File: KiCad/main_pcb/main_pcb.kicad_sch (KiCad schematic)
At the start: 14 parts, among them U4 SD Card Socket, U5 TI TXB0104DR, U6 TI TXB0104DR, U7 TI TXB0104DR, U9 ILI9488

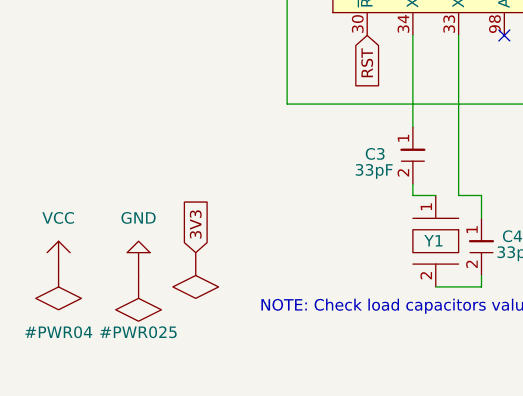
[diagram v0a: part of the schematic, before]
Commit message: feat(KiCad): Continues work on main PCB circuit
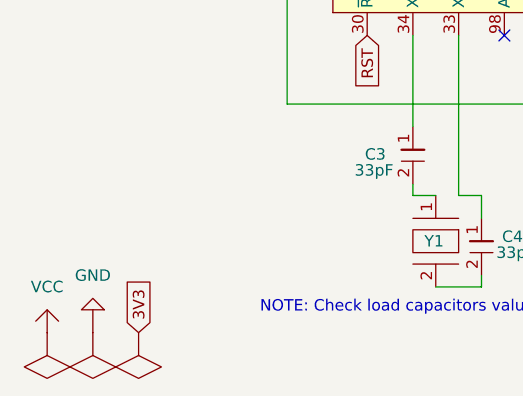
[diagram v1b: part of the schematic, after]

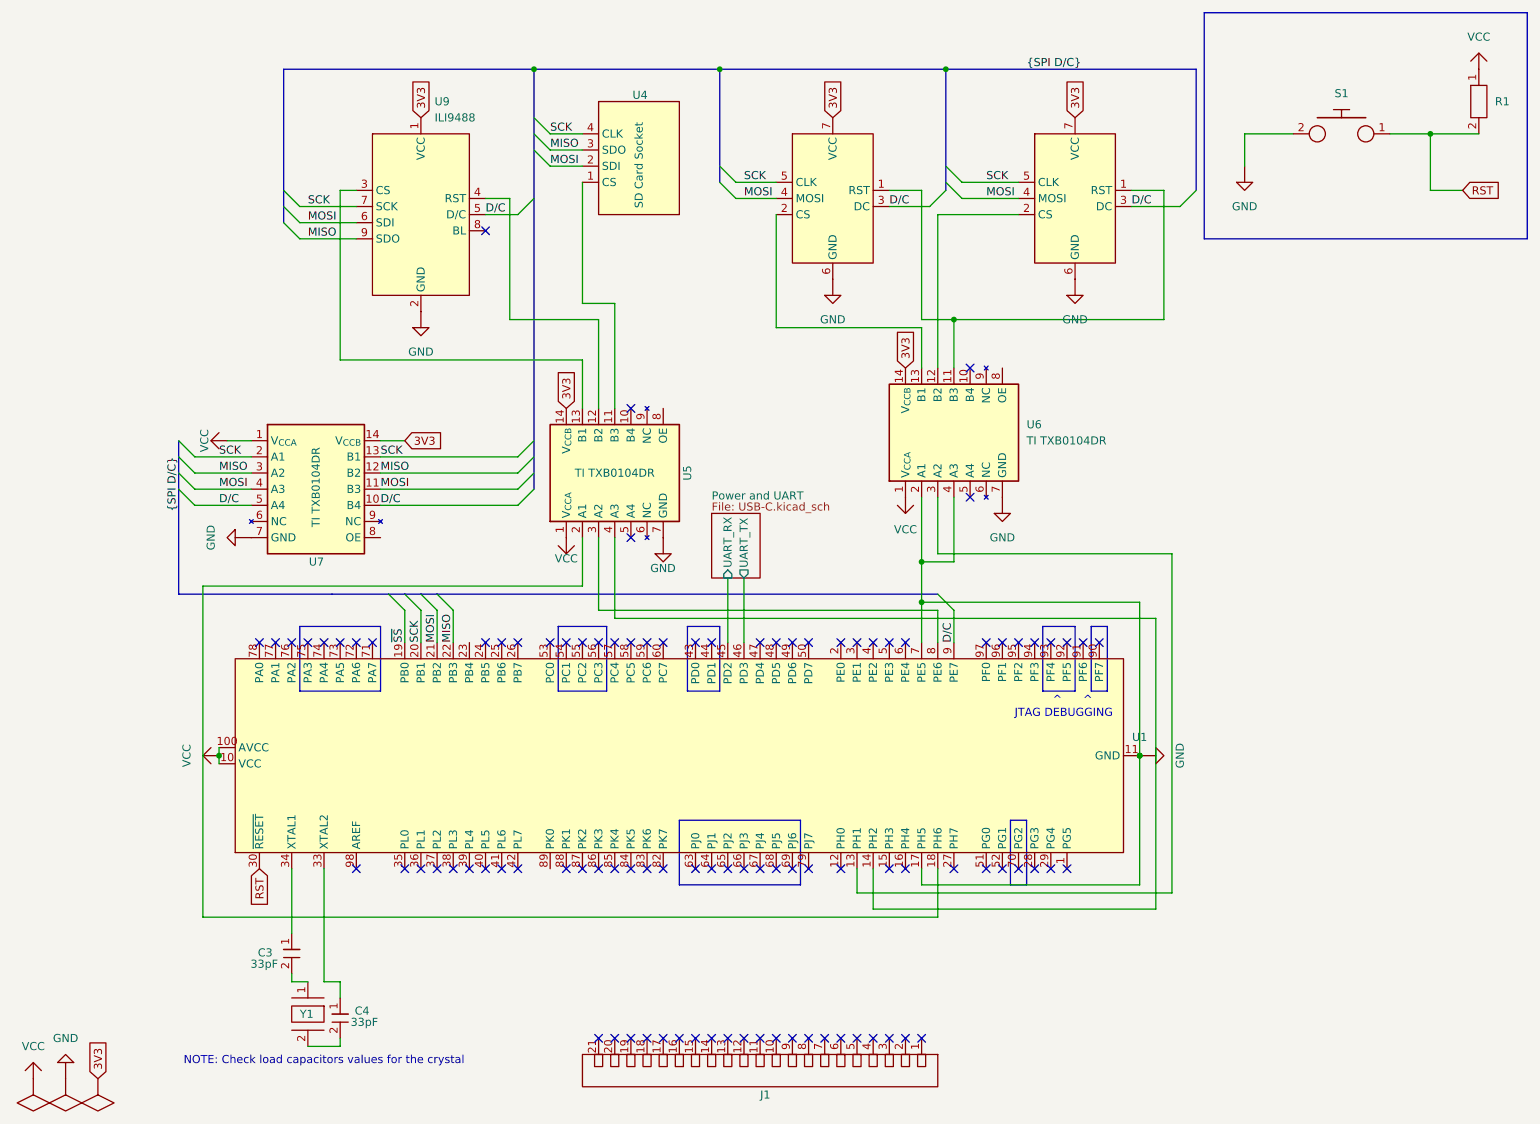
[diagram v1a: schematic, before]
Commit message: feat(KiCad): Continues work on main PCB circuit
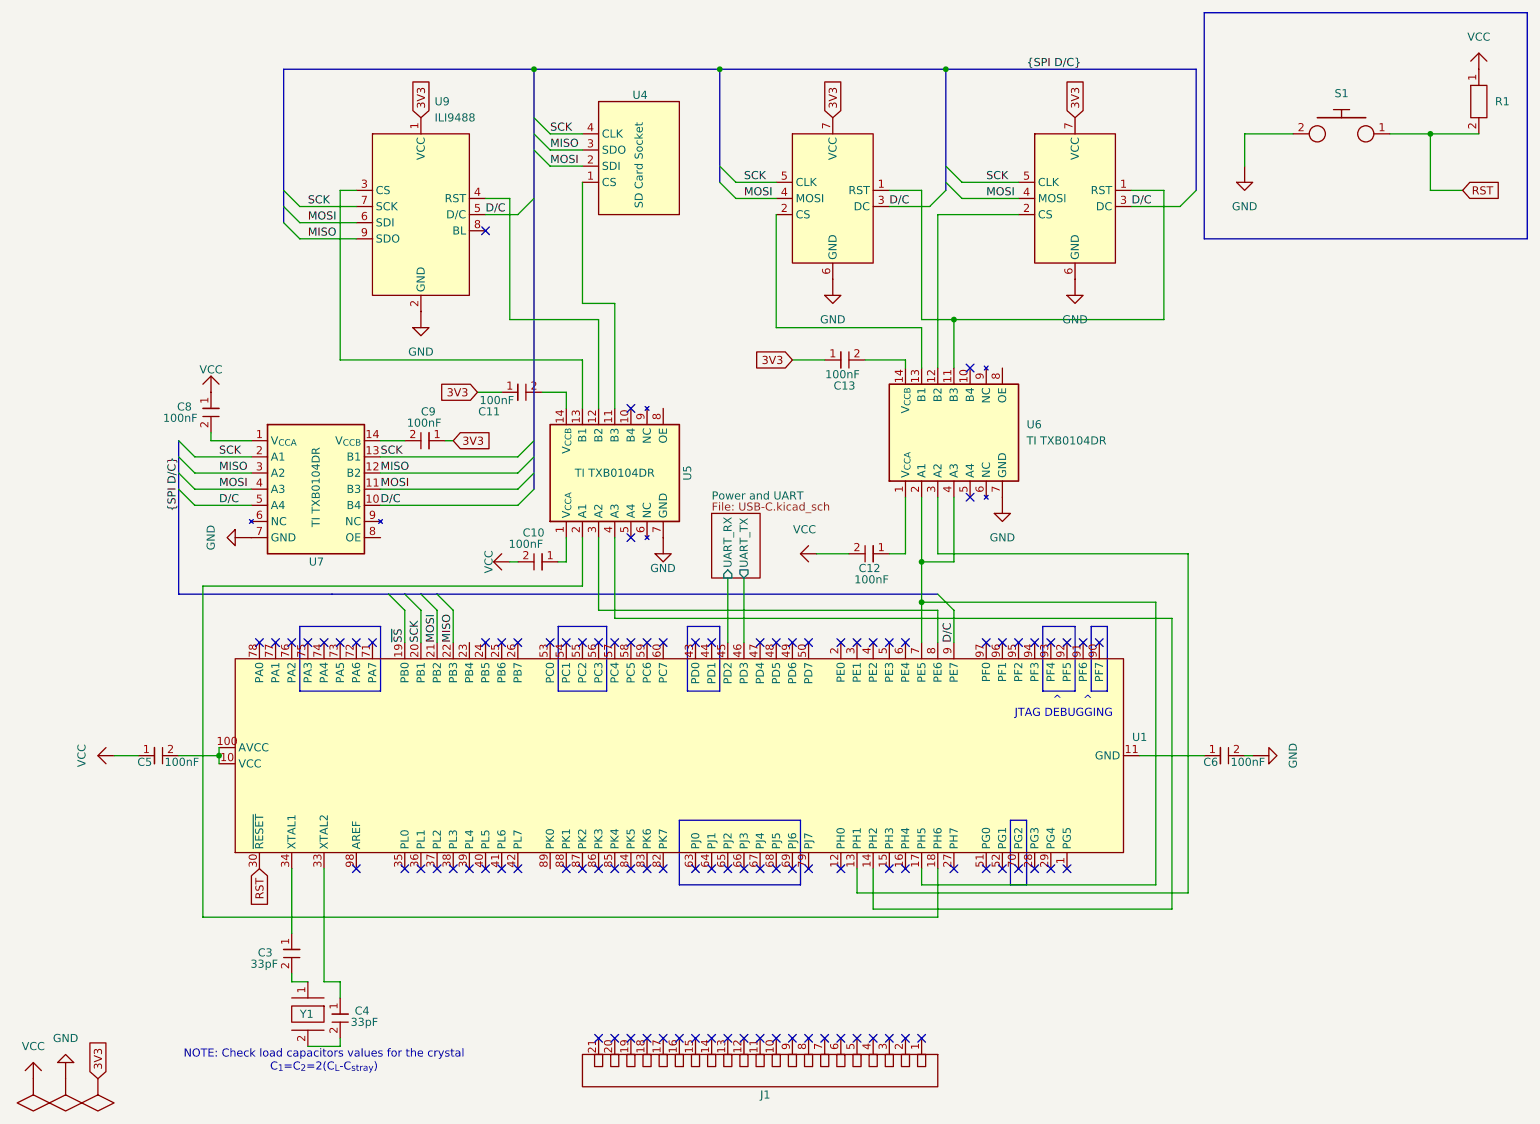
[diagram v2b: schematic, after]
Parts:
- added C10, C11, C12, C13, C5, C6, C8, C9: 100nF, symbol Lily's_Pad:Capacitor
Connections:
- net 3V3: now also C11.1, C13.1, C9.1; no longer U5.14 (V_{CCB}), U6.14 (V_{CCB}), U7.14 (V_{CCB})
- net GND: now also C6.1, C6.2; no longer U1.17 (PH5), U1.7 (PE5), U6.2 (A1), U6.4 (A3)
- net VCC: now also C10.2, C12.2, C5.1, C5.2, C8.1; no longer U5.1 (V_{CCA}), U6.1 (V_{CCA}), U7.1 (V_{CCA})
- new net: C8.2, U7.1 (V_{CCA})
- new net: C9.2, U7.14 (V_{CCB})
- new net: C11.2, U5.14 (V_{CCB})
- new net: C12.1, U6.1 (V_{CCA})
- new net: C10.1, U5.1 (V_{CCA})
- new net: C13.2, U6.14 (V_{CCB})
- new net: U1.17 (PH5), U1.7 (PE5), U6.2 (A1), U6.4 (A3)
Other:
- note added: "NOTE: Check load capacitors values for the crystal C_{1}=C_{2}=2(C_{L}-C_{stray})"
- note removed: "NOTE: Check load capacitors values for the crystal"

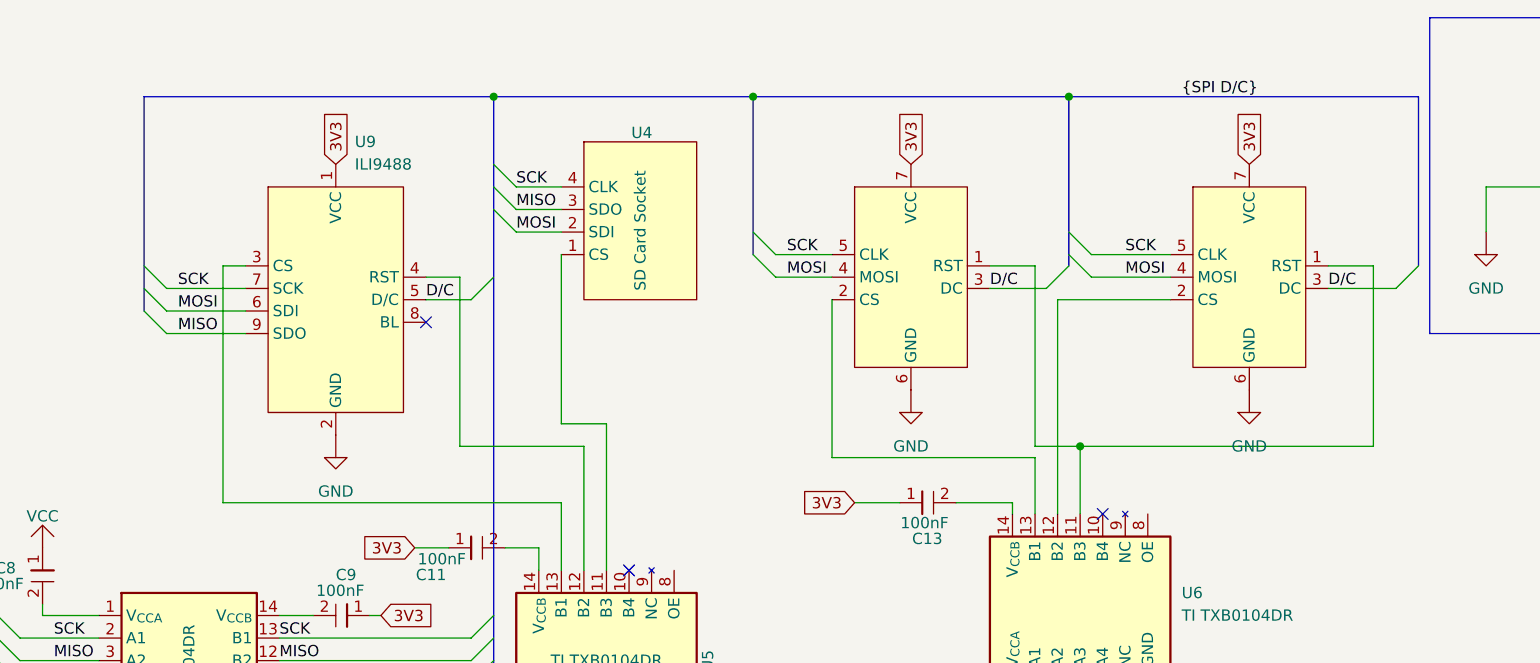
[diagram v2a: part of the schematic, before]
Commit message: feat(KiCad): Continues work on main PCB circuit
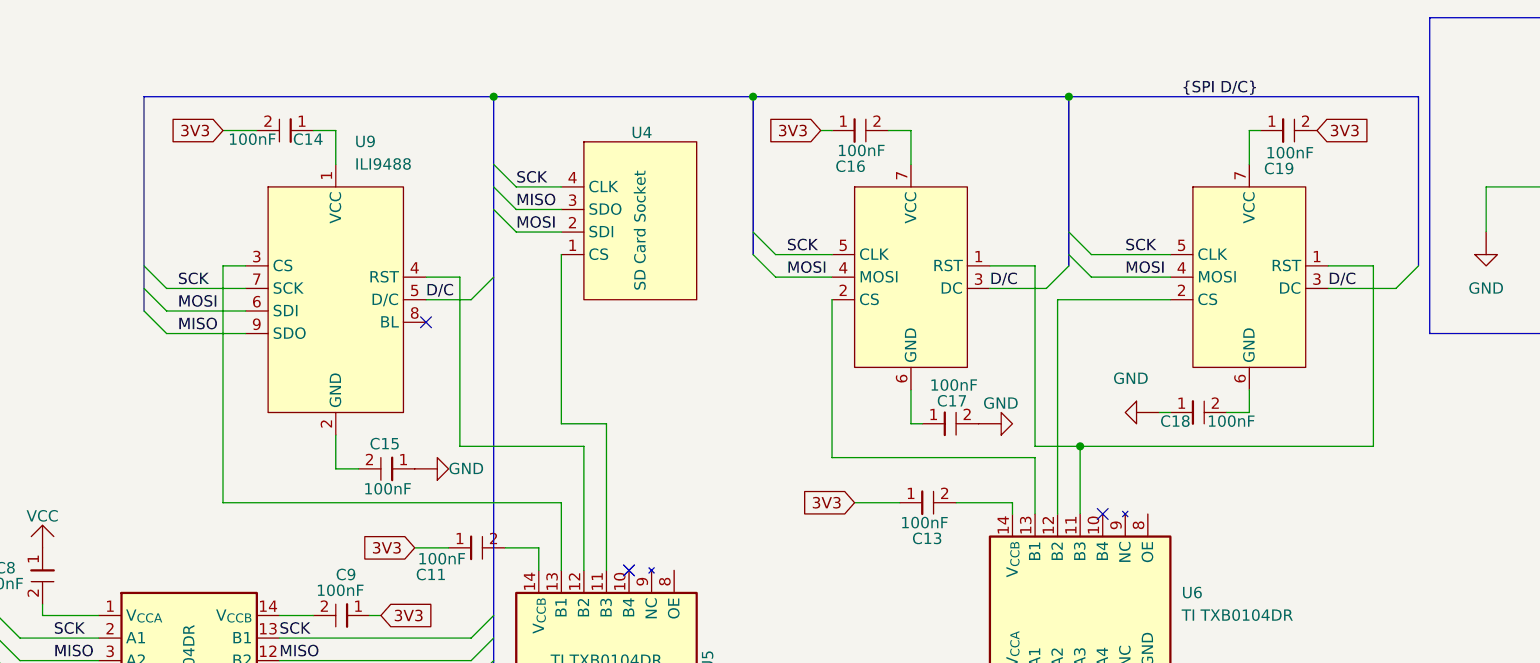
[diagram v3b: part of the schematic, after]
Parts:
- added C14, C15, C16, C17, C18, C19: 100nF, symbol Lily's_Pad:Capacitor
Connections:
- net 3V3: now also C14.2, C16.1, C19.2; no longer U2.7 (VCC), U3.7 (VCC), U9.1 (VCC)
- net GND: now also C15.1, C17.2, C18.1; no longer U2.6 (GND), U3.6 (GND), U9.2 (GND)
- new net: C18.2, U2.6 (GND)
- new net: C19.1, U2.7 (VCC)
- new net: C17.1, U3.6 (GND)
- new net: C16.2, U3.7 (VCC)
- new net: C14.1, U9.1 (VCC)
- new net: C15.2, U9.2 (GND)

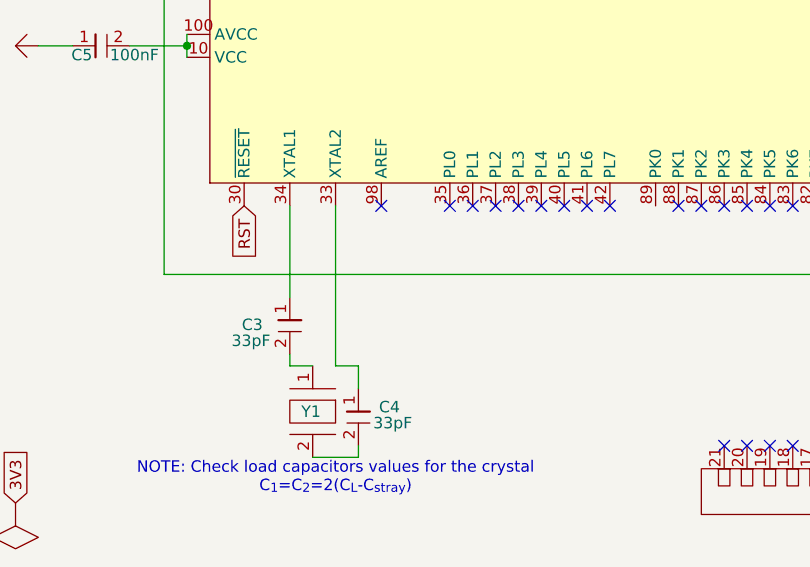
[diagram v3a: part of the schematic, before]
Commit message: feat(KiCad): Continues work on main PCB circuit
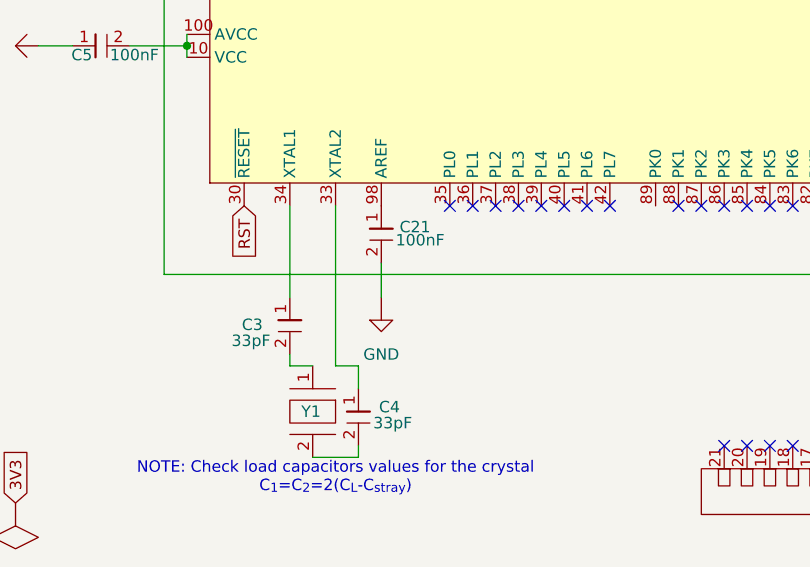
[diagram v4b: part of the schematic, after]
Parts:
- added C21: 100nF, symbol Lily's_Pad:Capacitor
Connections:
- net GND: now also C21.2
- no-connect marks 98 -> 97
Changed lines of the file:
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@@
 	)
 	(no_connect
-		(at 67.31 158.7501)
-	)
-	(no_connect
 		(at 171.45 158.7501)
 	)
@@
 	(wire
 		(pts
+			(xy 67.31 165.1) (xy 67.31 168.91)
+		)
+		(stroke
+			(width 0)
+			(type default)
+		)
+	)
+	(wire
+		(pts
 			(xy 44.45 91.44) (xy 50.8 91.44)
 		)
@@
 	)
 	(symbol
+		(lib_id "Lily's_Pad:Capacitor")
+		(at 67.31 162.56 0)
+		(unit 1)
+		(body_style 1)
+		(exclude_from_sim no)
+		(in_bom yes)
+		(on_board yes)
+		(in_pos_files yes)
+		(dnp no)
+		(property "Reference" "C21"
+			(at 69.342 161.0994 0)
+			(show_name no)
+			(do_not_autoplace no)
+			(effects
+				(font
+					(size 1.27 1.27)
+				)
+				(justify left)
+			)
+		)
+		(property "Value" "100nF"
+			(at 71.628 162.56 0)
+			(show_name no)
+			(do_not_autoplace no)
+			(effects
+				(font
+					(size 1.27 1.27)
+				)
+			)
+		)
+		(property "Footprint" ""
+			(at 67.31 162.56 0)
+			(hide yes)
+			(show_name no)
+			(do_not_autoplace no)
+			(effects
+				(font
+					(size 1.27 1.27)
+				)
+			)
+		)
+		(property "Datasheet" ""
+			(at 67.31 162.56 0)
+			(hide yes)
+			(show_name no)
+			(do_not_autoplace no)
+			(effects
+				(font
+					(size 1.27 1.27)
+				)
+			)
+		)
+		(property "Description" ""
+			(at 67.31 162.56 0)
+			(hide yes)
+			(show_name no)
+			(do_not_autoplace no)
+			(effects
+				(font
+					(size 1.27 1.27)
+				)
+			)
+		)
+		(pin "2"
+		)
+		(pin "1"
+		)
+		(instances
+			(project "main_pcb"
+				(path "/346fb29b-2426-4b69-9f9a-e979b6e41832"
+					(reference "C21")
+					(unit 1)
+				)
+			)
+		)
+	)
+	(symbol
 		(lib_id "Lily's_Pad:GND")
 		(at 207.01 50.8 0)
@@
 					(unit 1)
 				)
+			)
+		)
+	)
+	(symbol
+		(lib_id "Lily's_Pad:GND")
+		(at 67.31 171.45 0)
+		(unit 1)
+		(body_style 1)
+		(exclude_from_sim no)
+		(in_bom no)
+		(on_board no)
+		(in_pos_files yes)
+		(dnp no)
+		(fields_autoplaced yes)
+		(property "Reference" "#PWR028"
+			(at 67.31 173.99 0)
+			(hide yes)
+			(show_name no)
+			(do_not_autoplace no)
+			(effects
+				(font
+					(size 1.27 1.27)
+				)
+			)
+		)
+		(property "Value" "GND"
+			(at 67.31 175.26 0)
+			(show_name no)
+			(do_not_autoplace no)
+			(effects
+				(font
+					(size 1.27 1.27)
+				)
+			)
+		)
+		(property "Footprint" ""
+			(at 67.31 171.45 0)
+			(hide yes)
+			(show_name no)
+			(do_not_autoplace no)
+			(effects
+				(font
+					(size 1.27 1.27)
+				)
+			)
+		)
+		(property "Datasheet" ""
+			(at 67.31 171.45 0)
+			(hide yes)
+			(show_name no)
+			(do_not_autoplace no)
+			(effects
+				(font
+					(size 1.27 1.27)
+				)
+			)
+		)
+		(property "Description" ""
+			(at 67.31 171.45 0)
+			(hide yes)
+			(show_name no)
+			(do_not_autoplace no)
+			(effects
+				(font
+					(size 1.27 1.27)
+				)
+			)
+		)
+		(pin "1"
+		)
+		(instances
+			(project "main_pcb"
+				(path "/346fb29b-2426-4b69-9f9a-e979b6e41832"
+					(reference "#PWR028")
+					(unit 1)
+				)

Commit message: feat(KiCad): Continues work on circuit
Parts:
- C10, C11, C12, C13, C14, C15, C16, C17, C18, C19, C21, C3, C4, C5, C6, C8, C9: symbol Lily's_Pad:Capacitor -> lilys_pad:Capacitor
- J1: symbol Lily's_Pad:Header_21 -> lilys_pad:Header_21
- R1: symbol Lily's_Pad:Resistor -> lilys_pad:Resistor
- S1: symbol Lily's_Pad:Push-button_Switch -> lilys_pad:Push-button_Switch
- U1: symbol Lily's_Pad:ATmega_2560 -> lilys_pad:ATmega_2560
- U2, U3: symbol Lily's_Pad:GC9A01 -> lilys_pad:GC9A01
- U4: symbol Lily's_Pad:SD_Card_Socket -> lilys_pad:SD_Card_Socket
- U5, U6, U7: symbol Lily's_Pad:TI TXB0104DR -> lilys_pad:TI_TXB0104DR
- U9: symbol Lily's_Pad:ILI9488 -> lilys_pad:ILI9488
- Y1: symbol Lily's_Pad:Crystal -> lilys_pad:Crystal
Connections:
- net MISO: now also U1.22 (PB3), U4.2 (SDO); no longer U4.3 (SDO)
- net MOSI: now also U1.21 (PB2), U4.3 (SDI); no longer U4.2 (SDI)
- net SCK: now also U1.20 (PB1), U4.1 (CLK); no longer U4.4 (CLK)
- net ~{SS}: now also U1.19 (PB0)
- net at U5.11 (B3): now also U4.4 (CS); no longer U4.1 (CS)
- net at U1.98 (AREF): now also C21.1
- no-connect marks 97 -> 101
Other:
- moved on the sheet: C10, Y1

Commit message: feat(KiCad): Continues work on circuit
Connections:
- no-connect marks 101 -> 103

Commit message: feat(KiCad): Continues work on circuit
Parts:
- added R4, R5, R6, R7: 10kΩ, symbol lilys_pad:Resistor
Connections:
- net at U2.2 (CS): now also R7.2; no longer U6.12 (B2)
- net at U3.2 (CS): now also R6.1; no longer U6.13 (B1)
- net at U5.11 (B3): now also R5.1; no longer U4.4 (CS)
- net at U5.13 (B1): now also R4.1; no longer U9.3 (CS)
- new net: R5.2, U4.4 (CS)
- new net: R4.2, U9.3 (CS)
- new net: R6.2, U6.13 (B1)
- new net: R7.1, U6.12 (B2)
